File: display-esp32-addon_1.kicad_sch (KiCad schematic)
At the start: 6 parts, among them J1 Conn_01x07_Socket, J2 Conn_01x07_Socket

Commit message: agregando numero de parte a los conectores principales
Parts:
- J1, J2: LCSC Part (none) -> C2832270; Manufacturer (none) -> XFCN; Mfr. Part (none) -> PM254V-11-07-H85; Price (none) -> 0.1296
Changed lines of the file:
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@@
       (effects (font (size 1.27 1.27)) hide)
     )
-    (property "LCSC Part" "" (at 130.81 177.8 0)
+    (property "LCSC Part" "C2832270" (at 130.81 177.8 0)
       (effects (font (size 1.27 1.27)) hide)
     )
-    (property "Mfr. Part" "" (at 130.81 177.8 0)
+    (property "Mfr. Part" "PM254V-11-07-H85" (at 130.81 177.8 0)
       (effects (font (size 1.27 1.27)) hide)
     )
-    (property "Manufacturer" "" (at 130.81 177.8 0)
+    (property "Manufacturer" "XFCN" (at 130.81 177.8 0)
       (effects (font (size 1.27 1.27)) hide)
     )
-    (property "Description" "" (at 130.81 177.8 0)
+    (property "Description" "2.54mm Plugin 3A 7P -40℃~+105℃ 250V Straight 1x7P Top Square Holes Plugin,P=2.54mm Female Headers ROHS" (at 130.81 177.8 0)
       (effects (font (size 1.27 1.27)) hide)
     )
-    (property "Price" "" (at 130.81 177.8 0)
+    (property "Price" "0.1296" (at 130.81 177.8 0)
       (effects (font (size 1.27 1.27)) hide)
     )
@@
       (effects (font (size 1.27 1.27)) hide)
     )
-    (property "LCSC Part" "" (at 115.57 177.8 0)
+    (property "LCSC Part" "C2832270" (at 115.57 177.8 0)
       (effects (font (size 1.27 1.27)) hide)
     )
-    (property "Mfr. Part" "" (at 115.57 177.8 0)
+    (property "Mfr. Part" "PM254V-11-07-H85" (at 115.57 177.8 0)
       (effects (font (size 1.27 1.27)) hide)
     )
-    (property "Manufacturer" "" (at 115.57 177.8 0)
+    (property "Manufacturer" "XFCN" (at 115.57 177.8 0)
       (effects (font (size 1.27 1.27)) hide)
     )
-    (property "Description" "" (at 115.57 177.8 0)
+    (property "Description" "2.54mm Plugin 3A 7P -40℃~+105℃ 250V Straight 1x7P Top Square Holes Plugin,P=2.54mm Female Headers ROHS" (at 115.57 177.8 0)
       (effects (font (size 1.27 1.27)) hide)
     )
-    (property "Price" "" (at 115.57 177.8 0)
+    (property "Price" "0.1296" (at 115.57 177.8 0)
       (effects (font (size 1.27 1.27)) hide)
     )

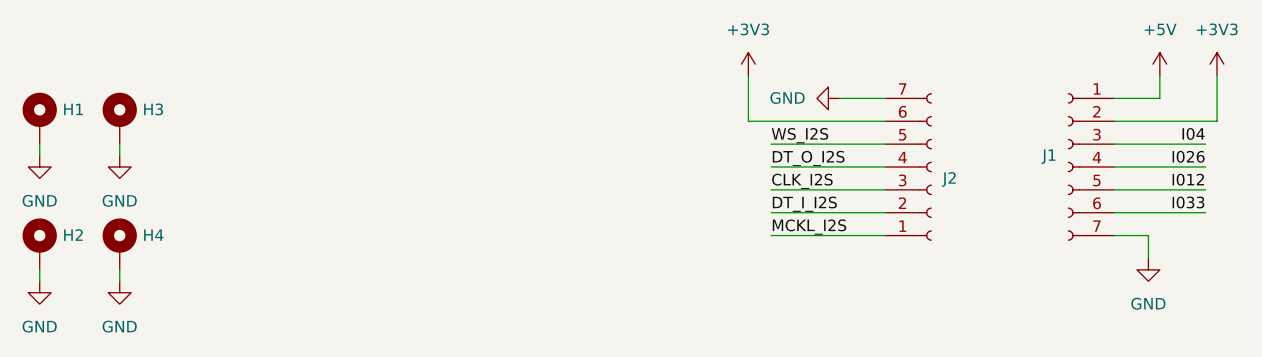
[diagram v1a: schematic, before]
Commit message: agregando fiducials
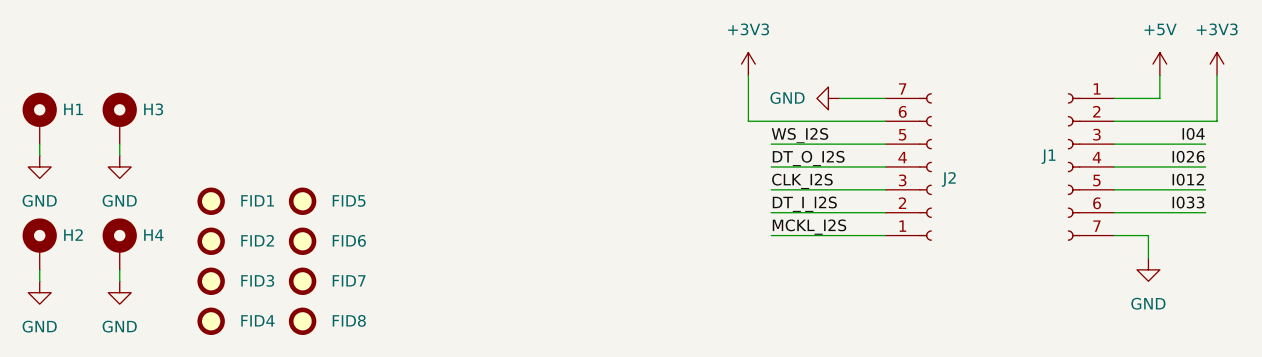
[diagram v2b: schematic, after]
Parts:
- added FID1, FID2, FID3, FID4, FID5, FID6, FID7, FID8: Fiducial, Fiducial:Fiducial_1mm_Mask2mm, symbol Mechanical:Fiducial
